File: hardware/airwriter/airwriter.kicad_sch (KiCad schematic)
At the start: 129 parts, among them J1 USB-C 5V in, J2 Mini-DIN-8 to printer, J4 Mini-DIN-8 LocalTalk, SW1 EVQP44B3M side-press, SW2 B3U-1000P, SW3 TS-1002-BR16026, U1 ESP32-S3-WROOM-1-N8R2, U2 MAX3490ESA+, U3 MAX3232ESE+, U4 AP7361C-33E, U5 USBLC6-2SC6, U6 SP3485EN-L, U7 PIC12F1840-I/P, U8 SP3485EN-L, U9 74AHCT1G125SE-7

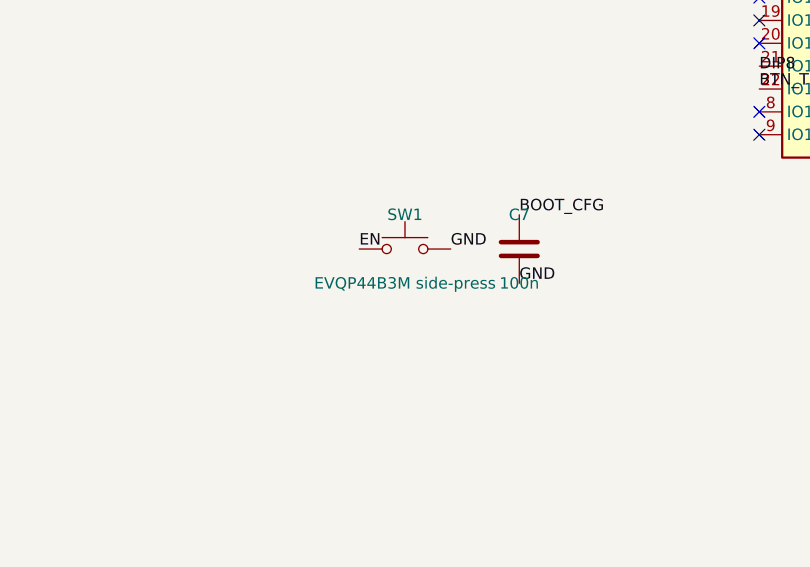
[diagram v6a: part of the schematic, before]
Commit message: Round 10: relocate reset (SW1) beside U1, match BOOT as B3U-1000P
Both service switches (reset SW1, boot SW2) now live near the ESP32 with
case-BOTTOM access, both Omron B3U-1000P top-tact (LCSC C231329). SW1's
side-press footprint is dropped -- pointless once interior/bottom-access,
and matched switches are cleaner. The west edge now carries only the DIP
S1 (relieves the S1<->SW1 tightness). This also makes both switch traces
short + fully routable. SW1 stays on /EN; SW2 on /BOOT_CFG (IO0).
Plan-4: no west-edge reset pinhole; two bottom buttons by U1.
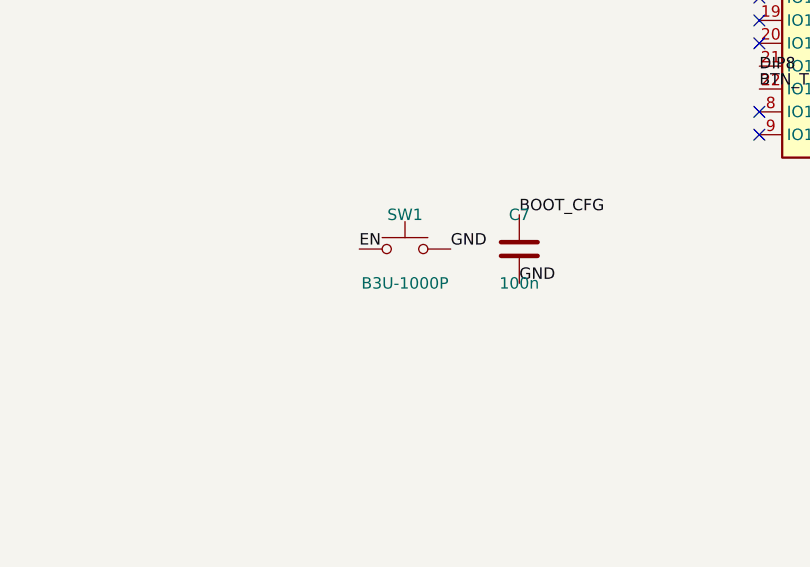
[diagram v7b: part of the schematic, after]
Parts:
- SW1: value EVQP44B3M side-press -> B3U-1000P; footprint airwriter:EVQP44B3M_SidePress -> Button_Switch_SMD:SW_SPST_B3U-1000P; LCSC C79164 -> C231329; Manufacturer none - bare pads on the board -> Omron

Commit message: Round 10 WIP: Wells's GUI routing (BOOT, R20, C67, EN cluster); reset restored to side-press at west edge, EN route pending
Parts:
- SW1: footprint Button_Switch_SMD:SW_SPST_B3U-1000P -> airwriter:EVQP44B3M_SidePress
